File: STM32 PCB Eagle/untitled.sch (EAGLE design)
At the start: 17 parts, among them IC1 LTV-846S, U1 SN65HVD230/1

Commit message: Added serial debug hdr and minor rerouting
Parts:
- added H1: 1X2, headers(.1in):1X2
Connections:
- new net RX1: H1.2, STM32.PA10/RX1
- new net TX1: H1.1, STM32.PA9/TX1
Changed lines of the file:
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@@
 <part name="U$1" library="headers(2mm)" deviceset="1X8" device=""/>
 <part name="R9" library="rcl" library_urn="urn:adsk.eagle:library:334" deviceset="R-EU_" device="R1206" package3d_urn="urn:adsk.eagle:package:23540/2" value="47k ohm"/>
+<part name="H1" library="headers(.1in)" deviceset="1X2" device=""/>
 </parts>
 <sheets>
@@
 <attribute name="NAME" x="115.57" y="85.3186" size="1.778" layer="95"/>
 </instance>
+<instance part="H1" gate="G$1" x="0" y="83.82" smashed="yes">
+<attribute name="NAME" x="-2.54" y="86.995" size="1.27" layer="95" font="vector"/>
+<attribute name="VALUE" x="-2.54" y="76.835" size="1.27" layer="96" font="vector"/>
+</instance>
 </instances>
 <busses>
@@
 <pinref part="STM32" gate="G$1" pin="PB9"/>
 <wire x1="20.32" y1="45.72" x2="17.78" y2="45.72" width="0.1524" layer="91"/>
-<label x="10.16" y="43.18" size="1.778" layer="95"/>
+<label x="10.16" y="45.72" size="1.778" layer="95"/>
 </segment>
 </net>
@@
 </segment>
 </net>
+<net name="TX1" class="0">
+<segment>
+<pinref part="H1" gate="G$1" pin="1"/>
+<wire x1="2.54" y1="83.82" x2="10.16" y2="83.82" width="0.1524" layer="91"/>
+<wire x1="10.16" y1="83.82" x2="10.16" y2="73.66" width="0.1524" layer="91"/>
+<pinref part="STM32" gate="G$1" pin="PA9/TX1"/>
+<wire x1="10.16" y1="73.66" x2="20.32" y2="73.66" width="0.1524" layer="91"/>
+<label x="2.54" y="83.82" size="1.778" layer="95"/>
+</segment>
+</net>
+<net name="RX1" class="0">
+<segment>
+<pinref part="STM32" gate="G$1" pin="PA10/RX1"/>
+<wire x1="20.32" y1="71.12" x2="7.62" y2="71.12" width="0.1524" layer="91"/>
+<wire x1="7.62" y1="71.12" x2="7.62" y2="81.28" width="0.1524" layer="91"/>
+<pinref part="H1" gate="G$1" pin="2"/>
+<wire x1="7.62" y1="81.28" x2="2.54" y2="81.28" width="0.1524" layer="91"/>
+<label x="2.54" y="81.28" size="1.778" layer="95"/>
+</segment>
+</net>

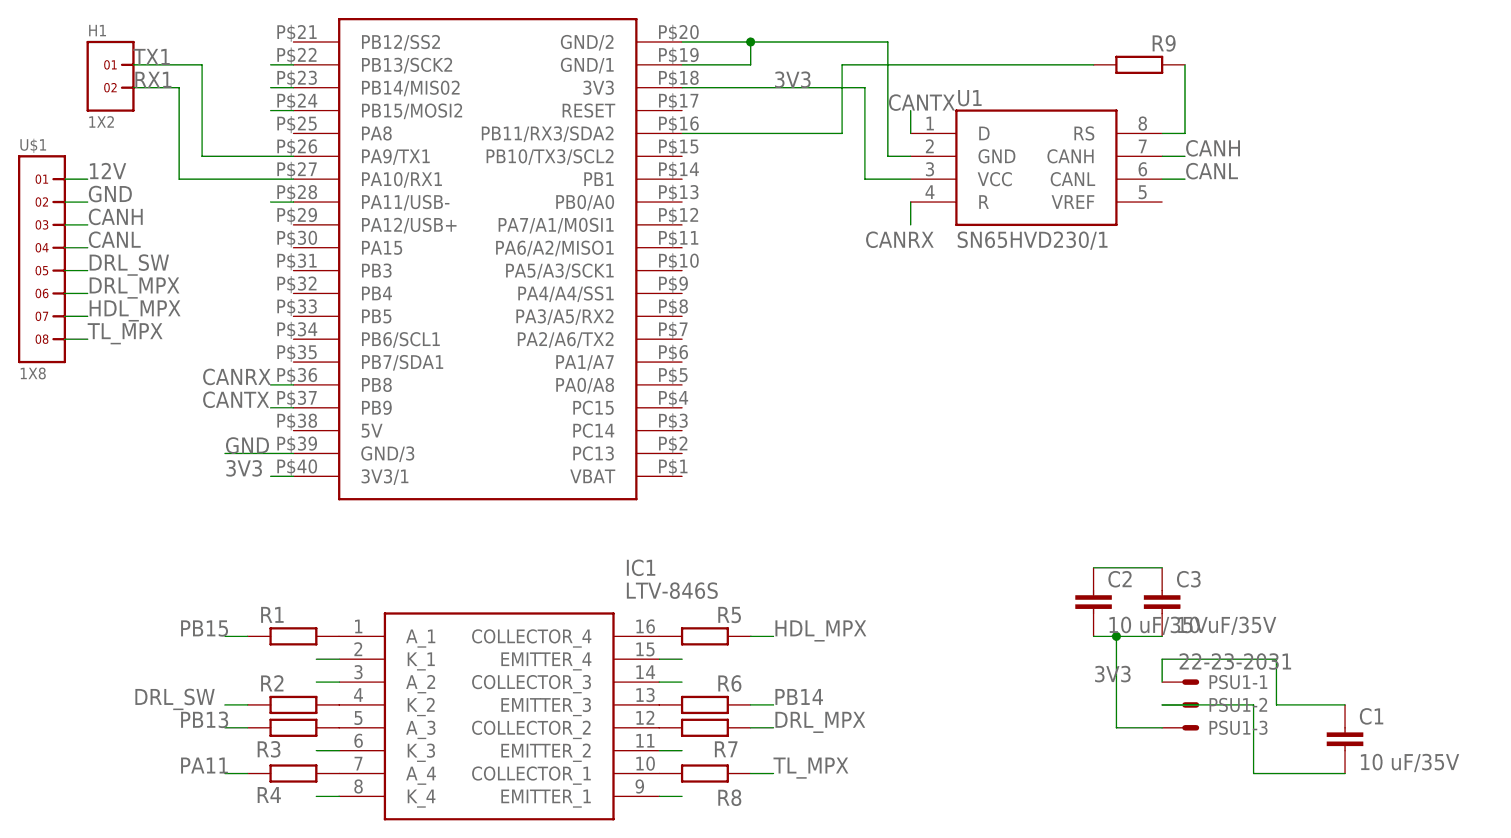
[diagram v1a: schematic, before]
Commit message: Alterations to keep MPX resistance below 200 ohms
The MPX only allows a resistance of < 250 ohms. I've made the following alterations to keep the LTV-846 resistance to MPX ~200 ohms. The resistors between the LTV-846 and the MPX were there only to reduce current through the LTV. In conditions I've observed, the LTV-846 should be under it's maximum ratings without the resistors. If the current draw through the LTV-846 spikes for some reason, there is no risk to the MPX or STM32.
Removing these resistors should have no detrimental impact.
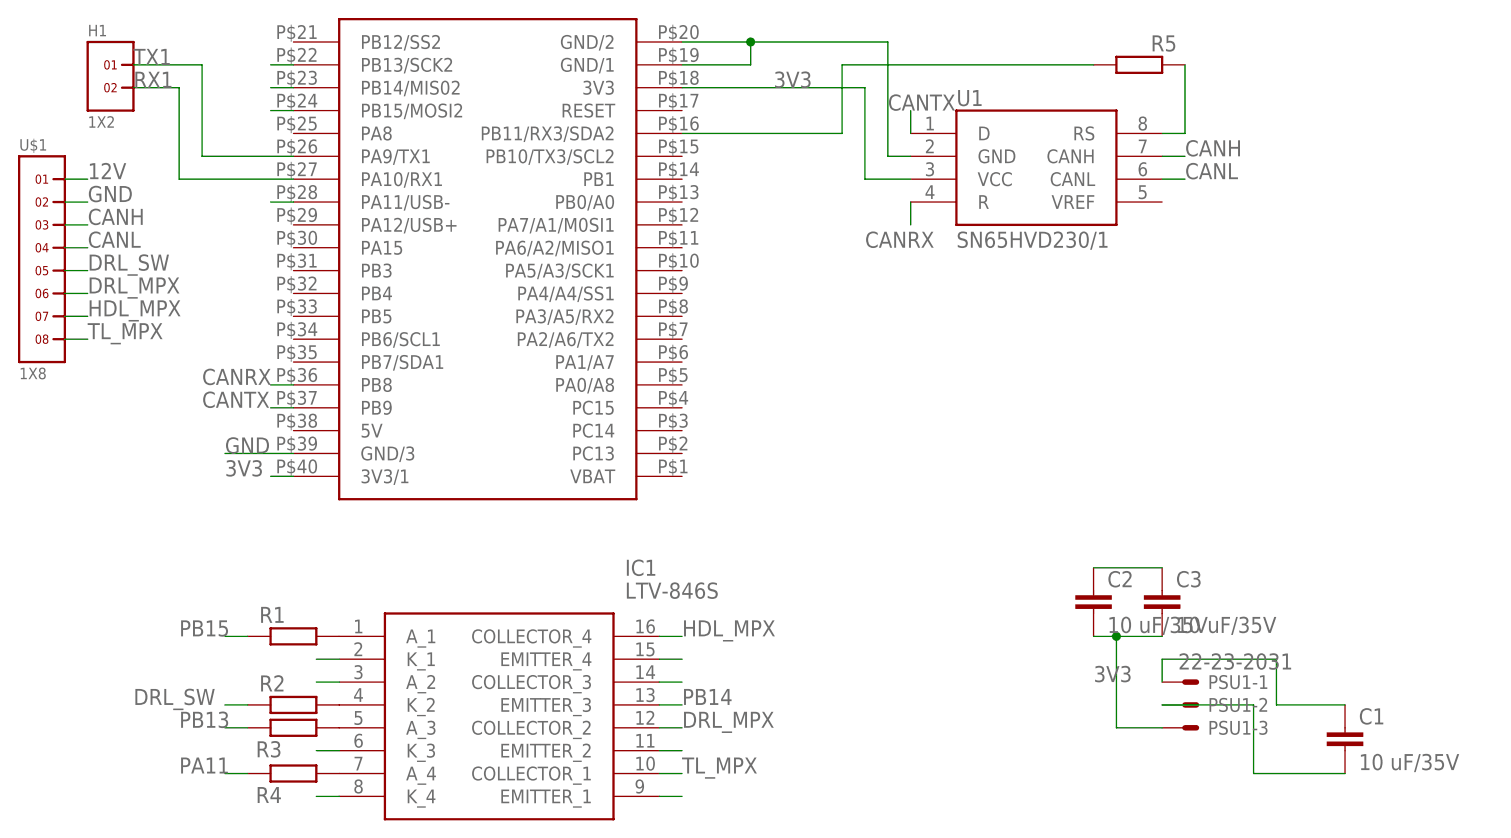
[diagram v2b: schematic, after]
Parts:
- removed R6, R9: 47k ohm, rcl:R-EU_R1206
- removed R7, R8: 1k ohm, rcl:R-EU_R1206
- R1, R3, R4: value 1k ohm -> 47 ohm
- R5: value 1k ohm -> 47k ohm
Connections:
- removed net N$1: IC1.COLLECTOR_4, R5.1
- removed net N$3: IC1.EMITTER_3, R6.1
- removed net N$5: IC1.COLLECTOR_2, R7.1
- removed net N$7: IC1.COLLECTOR_1, R8.1
- net DRL_MPX: now also IC1.COLLECTOR_2; no longer R7.2
- net HDL_MPX: now also IC1.COLLECTOR_4; no longer R5.2
- net N$9: now also R5.2; no longer R9.2
- net PB11: now also R5.1; no longer R9.1
- net PB14: now also IC1.EMITTER_3; no longer R6.2
- net TL_MPX: now also IC1.COLLECTOR_1; no longer R8.2
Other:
- moved on the sheet: R5
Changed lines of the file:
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@@
 <part name="C2" library="eagle-ltspice" library_urn="urn:adsk.eagle:library:217" deviceset="C" device="C1206" package3d_urn="urn:adsk.eagle:package:13279/1" value="10 uF/35V"/>
 <part name="C3" library="eagle-ltspice" library_urn="urn:adsk.eagle:library:217" deviceset="C" device="C1206" package3d_urn="urn:adsk.eagle:package:13279/1" value="10 uF/35V"/>
-<part name="R1" library="rcl" library_urn="urn:adsk.eagle:library:334" deviceset="R-EU_" device="R1206" package3d_urn="urn:adsk.eagle:package:23540/2" value="1k ohm"/>
+<part name="R1" library="rcl" library_urn="urn:adsk.eagle:library:334" deviceset="R-EU_" device="R1206" package3d_urn="urn:adsk.eagle:package:23540/2" value="47 ohm"/>
 <part name="R2" library="rcl" library_urn="urn:adsk.eagle:library:334" deviceset="R-EU_" device="R1206" package3d_urn="urn:adsk.eagle:package:23540/2" value="1k ohm"/>
-<part name="R3" library="rcl" library_urn="urn:adsk.eagle:library:334" deviceset="R-EU_" device="R1206" package3d_urn="urn:adsk.eagle:package:23540/2" value="1k ohm"/>
-<part name="R4" library="rcl" library_urn="urn:adsk.eagle:library:334" deviceset="R-EU_" device="R1206" package3d_urn="urn:adsk.eagle:package:23540/2" value="1k ohm"/>
-<part name="R5" library="rcl" library_urn="urn:adsk.eagle:library:334" deviceset="R-EU_" device="R1206" package3d_urn="urn:adsk.eagle:package:23540/2" value="1k ohm"/>
-<part name="R6" library="rcl" library_urn="urn:adsk.eagle:library:334" deviceset="R-EU_" device="R1206" package3d_urn="urn:adsk.eagle:package:23540/2" value="47k ohm"/>
-<part name="R7" library="rcl" library_urn="urn:adsk.eagle:library:334" deviceset="R-EU_" device="R1206" package3d_urn="urn:adsk.eagle:package:23540/2" value="1k ohm"/>
-<part name="R8" library="rcl" library_urn="urn:adsk.eagle:library:334" deviceset="R-EU_" device="R1206" package3d_urn="urn:adsk.eagle:package:23540/2" value="1k ohm"/>
+<part name="R3" library="rcl" library_urn="urn:adsk.eagle:library:334" deviceset="R-EU_" device="R1206" package3d_urn="urn:adsk.eagle:package:23540/2" value="47 ohm"/>
+<part name="R4" library="rcl" library_urn="urn:adsk.eagle:library:334" deviceset="R-EU_" device="R1206" package3d_urn="urn:adsk.eagle:package:23540/2" value="47 ohm"/>
 <part name="PSU1" library="con-molex" library_urn="urn:adsk.eagle:library:165" deviceset="22-23-2031" device="" package3d_urn="urn:adsk.eagle:package:8078634/1"/>
 <part name="IC1" library="LTV-846S" deviceset="LTV-846S" device=""/>
 <part name="U$1" library="headers(2mm)" deviceset="1X8" device=""/>
-<part name="R9" library="rcl" library_urn="urn:adsk.eagle:library:334" deviceset="R-EU_" device="R1206" package3d_urn="urn:adsk.eagle:package:23540/2" value="47k ohm"/>
+<part name="R5" library="rcl" library_urn="urn:adsk.eagle:library:334" deviceset="R-EU_" device="R1206" package3d_urn="urn:adsk.eagle:package:23540/2" value="47k ohm"/>
 <part name="H1" library="headers(.1in)" deviceset="1X2" device=""/>
 </parts>
@@
 <attribute name="NAME" x="19.05" y="3.5814" size="1.778" layer="95" rot="R180"/>
 </instance>
-<instance part="R5" gate="G$1" x="66.04" y="20.32" smashed="yes">
-<attribute name="NAME" x="67.31" y="21.8186" size="1.778" layer="95"/>
-</instance>
-<instance part="R6" gate="G$1" x="66.04" y="12.7" smashed="yes">
-<attribute name="NAME" x="67.31" y="14.1986" size="1.778" layer="95"/>
-</instance>
-<instance part="R7" gate="G$1" x="66.04" y="10.16" smashed="yes">
-<attribute name="NAME" x="69.85" y="8.6614" size="1.778" layer="95" rot="R180"/>
-</instance>
-<instance part="R8" gate="G$1" x="66.04" y="5.08" smashed="yes">
-<attribute name="NAME" x="67.31" y="1.4986" size="1.778" layer="95"/>
-</instance>
 <instance part="PSU1" gate="-1" x="119.38" y="15.24" smashed="yes">
 <attribute name="NAME" x="121.92" y="14.478" size="1.524" layer="95"/>
@@
 <attribute name="VALUE" x="-10.16" y="48.895" size="1.27" layer="96" font="vector"/>
 </instance>
-<instance part="R9" gate="G$1" x="114.3" y="83.82" smashed="yes">
+<instance part="R5" gate="G$1" x="114.3" y="83.82" smashed="yes">
 <attribute name="NAME" x="115.57" y="85.3186" size="1.778" layer="95"/>
 </instance>
@@
 <wire x1="63.5" y1="76.2" x2="81.28" y2="76.2" width="0.1524" layer="91"/>
 <wire x1="81.28" y1="76.2" x2="81.28" y2="83.82" width="0.1524" layer="91"/>
-<pinref part="R9" gate="G$1" pin="1"/>
+<pinref part="R5" gate="G$1" pin="1"/>
 <wire x1="81.28" y1="83.82" x2="109.22" y2="83.82" width="0.1524" layer="91"/>
 </segment>
@@
 </segment>
 <segment>
-<pinref part="R6" gate="G$1" pin="2"/>
-<wire x1="71.12" y1="12.7" x2="73.66" y2="12.7" width="0.1524" layer="91"/>
-<label x="73.66" y="12.7" size="1.778" layer="95"/>
+<wire x1="60.96" y1="12.7" x2="63.5" y2="12.7" width="0.1524" layer="91"/>
+<label x="63.5" y="12.7" size="1.778" layer="95"/>
+<pinref part="IC1" gate="G$1" pin="EMITTER_3"/>
 </segment>
 </net>
@@
 <net name="HDL_MPX" class="0">
 <segment>
-<pinref part="R5" gate="G$1" pin="2"/>
-<wire x1="71.12" y1="20.32" x2="73.66" y2="20.32" width="0.1524" layer="91"/>
-<label x="73.66" y="20.32" size="1.778" layer="95"/>
+<wire x1="60.96" y1="20.32" x2="63.5" y2="20.32" width="0.1524" layer="91"/>
+<label x="63.5" y="20.32" size="1.778" layer="95"/>
+<pinref part="IC1" gate="G$1" pin="COLLECTOR_4"/>
 </segment>
 <segment>
@@
 <net name="DRL_MPX" class="0">
 <segment>
-<pinref part="R7" gate="G$1" pin="2"/>
-<wire x1="71.12" y1="10.16" x2="73.66" y2="10.16" width="0.1524" layer="91"/>
-<label x="73.66" y="10.16" size="1.778" layer="95"/>
+<wire x1="60.96" y1="10.16" x2="63.5" y2="10.16" width="0.1524" layer="91"/>
+<label x="63.5" y="10.16" size="1.778" layer="95"/>
+<pinref part="IC1" gate="G$1" pin="COLLECTOR_2"/>
 </segment>
 <segment>
@@
 <net name="TL_MPX" class="0">
 <segment>
-<pinref part="R8" gate="G$1" pin="2"/>
-<wire x1="71.12" y1="5.08" x2="73.66" y2="5.08" width="0.1524" layer="91"/>
-<label x="73.66" y="5.08" size="1.778" layer="95"/>
+<wire x1="60.96" y1="5.08" x2="63.5" y2="5.08" width="0.1524" layer="91"/>
+<label x="63.5" y="5.08" size="1.778" layer="95"/>
+<pinref part="IC1" gate="G$1" pin="COLLECTOR_1"/>
 </segment>
 <segment>
@@
 </segment>
 </net>
-<net name="N$1" class="0">
-<segment>
-<pinref part="IC1" gate="G$1" pin="COLLECTOR_4"/>
-<pinref part="R5" gate="G$1" pin="1"/>
-</segment>
-</net>
 <net name="N$2" class="0">
 <segment>
@@
 </segment>
 </net>
-<net name="N$3" class="0">
-<segment>
-<pinref part="IC1" gate="G$1" pin="EMITTER_3"/>
-<pinref part="R6" gate="G$1" pin="1"/>
-</segment>
-</net>
 <net name="N$4" class="0">
 <segment>
@@
 </segment>
 </net>
-<net name="N$5" class="0">
-<segment>
-<pinref part="IC1" gate="G$1" pin="COLLECTOR_2"/>
-<pinref part="R7" gate="G$1" pin="1"/>
-</segment>
-</net>
 <net name="N$6" class="0">
 <segment>
 <pinref part="IC1" gate="G$1" pin="A_3"/>
 <pinref part="R3" gate="G$1" pin="2"/>
-</segment>
-</net>
-<net name="N$7" class="0">
-<segment>
-<pinref part="IC1" gate="G$1" pin="COLLECTOR_1"/>
-<pinref part="R8" gate="G$1" pin="1"/>
 </segment>
 </net>
@@
 <pinref part="U1" gate="G$1" pin="RS"/>
 <wire x1="116.84" y1="76.2" x2="119.38" y2="76.2" width="0.1524" layer="91"/>
-<pinref part="R9" gate="G$1" pin="2"/>
-</segment>
-</net>
+<pinref part="R5" gate="G$1" pin="2"/>
+</segment>
+</net>

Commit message: This is the version sent to printing.
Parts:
- H1: value 1X2 -> 1X3; device headers(.1in):1X2 -> headers(.1in):1X3
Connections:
- new net PA1: R5.1, STM32.PA1/A7
- net 12V: now also U$1.2; no longer U$1.1
- net CANH: now also U$1.7; no longer U$1.3
- net CANL: now also U$1.8; no longer U$1.4
- net GND: now also H1.3, U$1.1; no longer U$1.2
- net HDL_MPX: now also U$1.3; no longer U$1.7
- net PB11: no longer R5.1
- net TL_MPX: now also U$1.4; no longer U$1.8
